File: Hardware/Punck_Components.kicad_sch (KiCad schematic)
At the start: 115 parts, among them J1 Conn_01x12_Female, J2 Conn_01x12_Female, J3 Conn_01x12_Female, J4 Conn_01x12_Female, J6 SWD_Header, J7 Eurorack_10_pin_power, Q1 MMBT3904, Q2 MMBT3904, Q3 MMBT3904, Q4 MMBT3904, Q5 MMBT3904, Q6 MMBT3904, Q7 MMBT3904, U1 TL074, U2 STM32H743ZITx, U3 W25Q128JVS, U4 PCM5100APW, U5 W25Q128JVS, U6 TPS561201, U7 LD1117-3.3-4Tab, Y1 8MHz 20pF

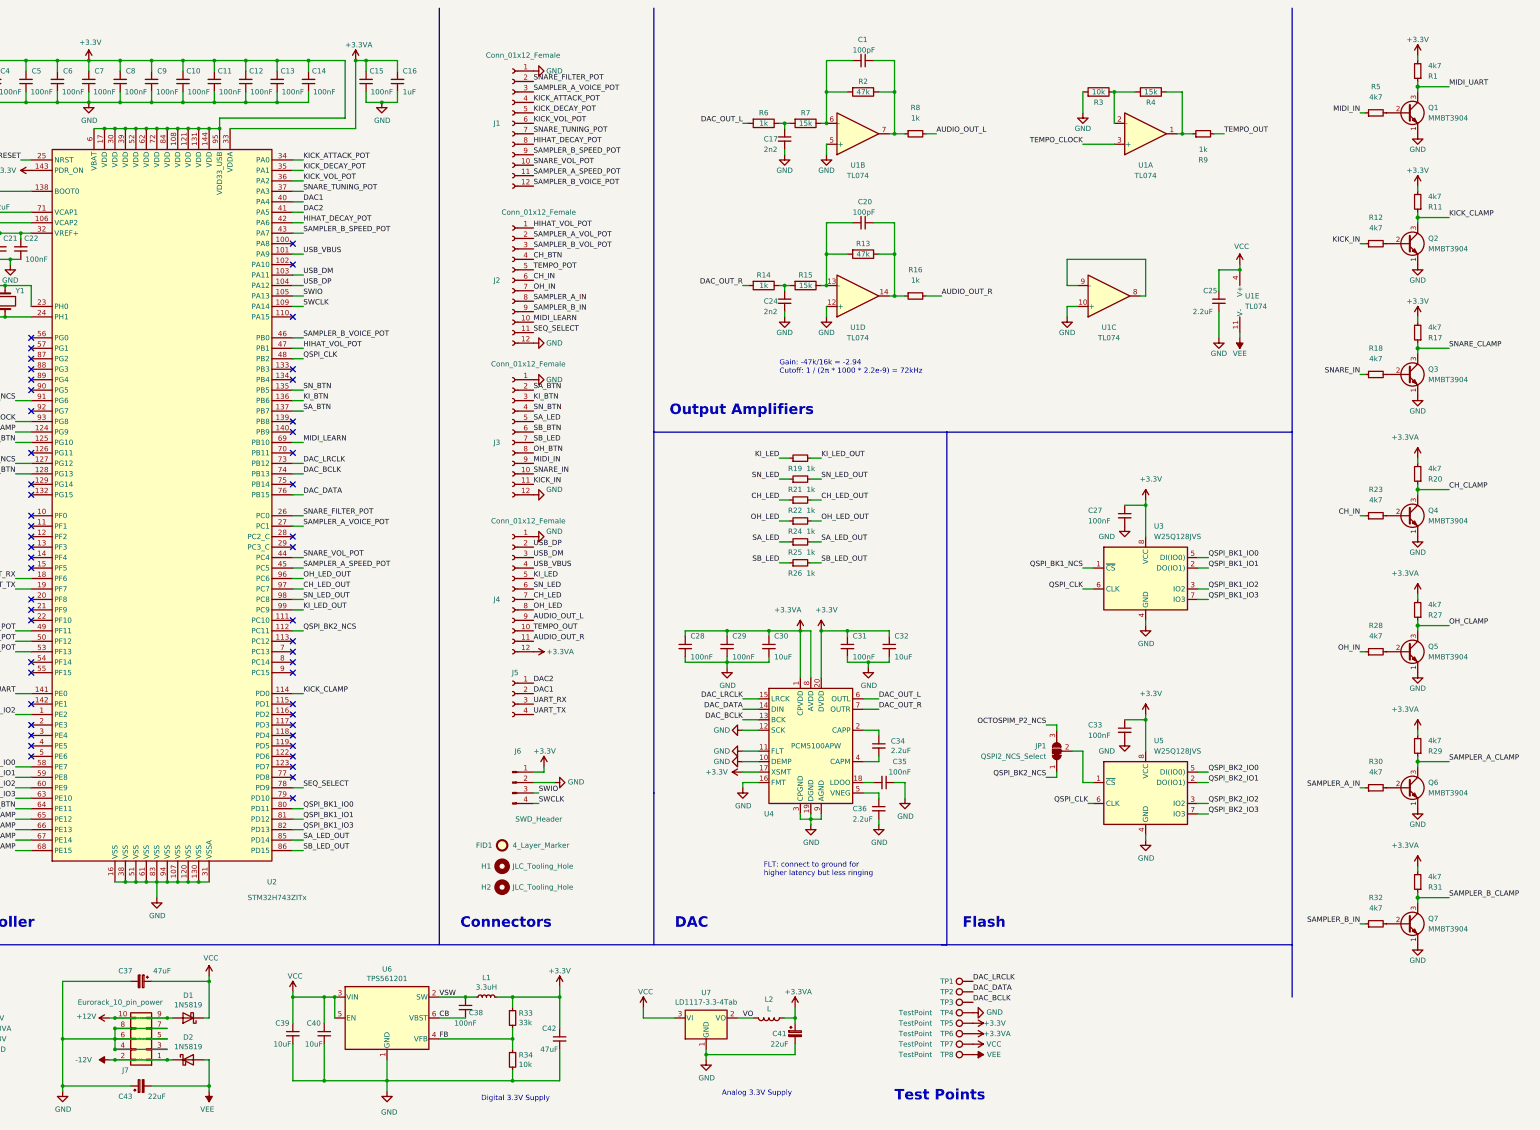
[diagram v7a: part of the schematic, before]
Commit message: Updated components on panel board
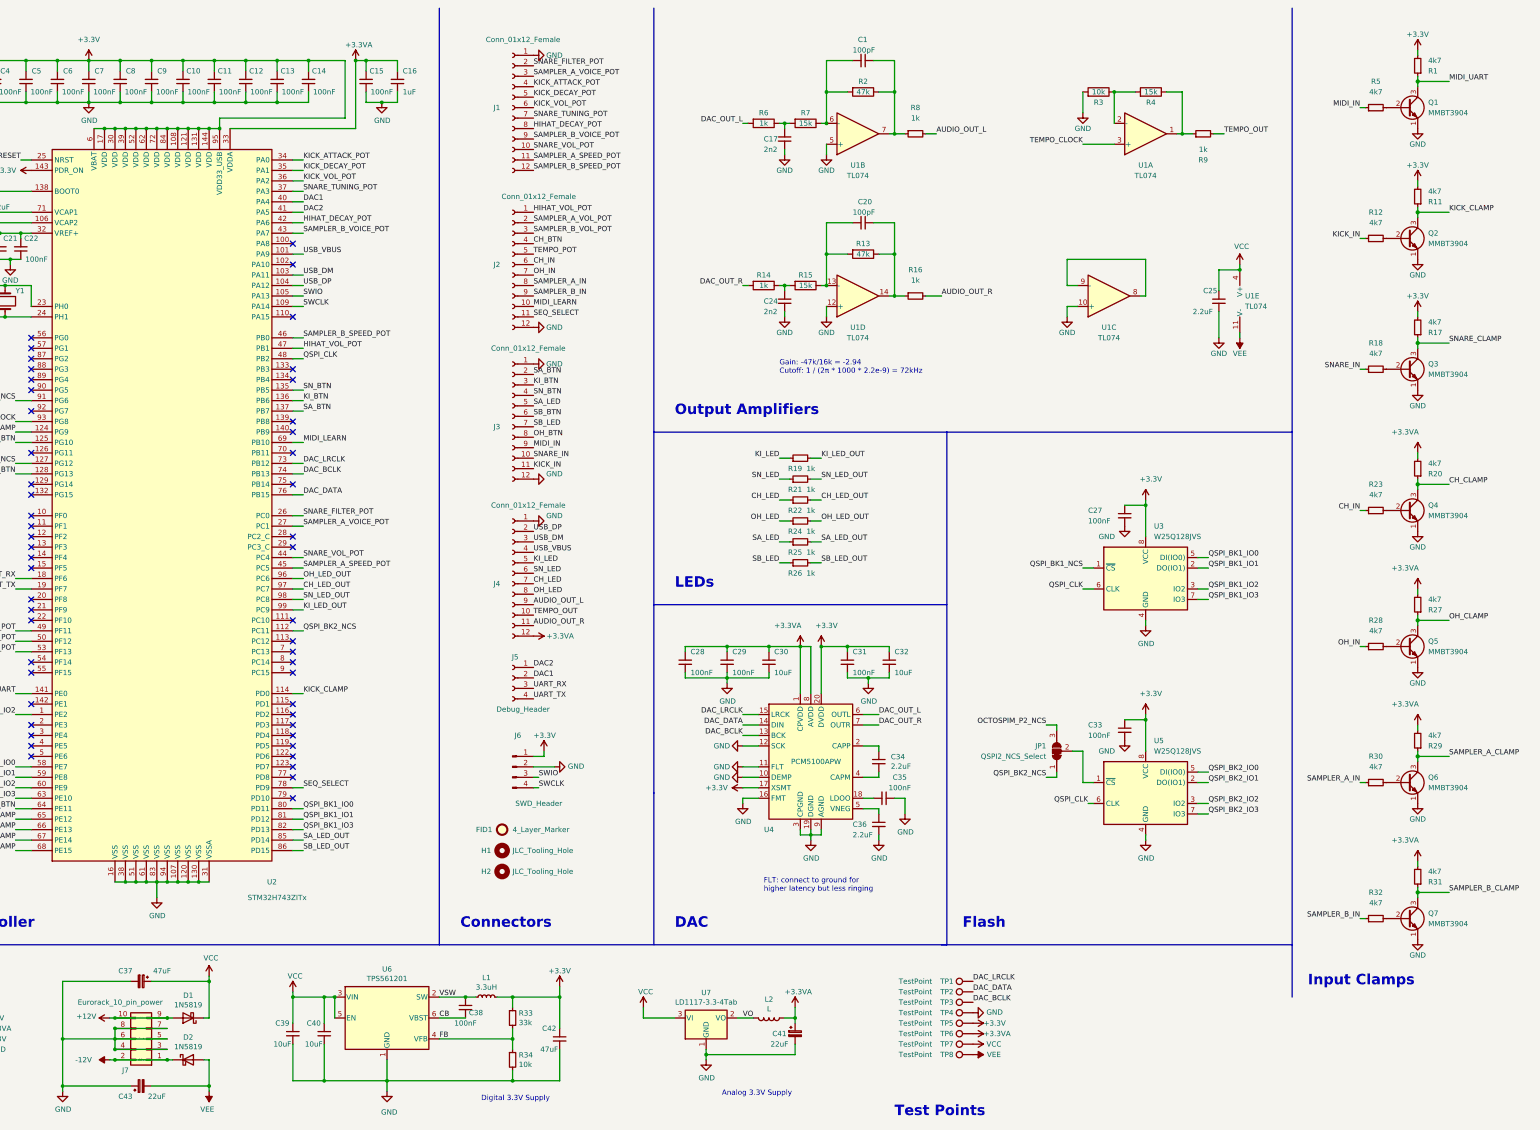
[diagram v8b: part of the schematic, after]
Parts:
- J5: value (none) -> Debug_Header
- TP1, TP2, TP3: value (none) -> TestPoint; footprint (none) -> Custom_Footprints:1.3mm_Test_Point
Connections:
- net +3V3: no longer C10.2, C11.2, C12.2, C13.2, C14.2, C2.2, C3.2, C31.1, C32.1, C4.2, C5.2, C6.2, C7.2, C8.2, C9.2, U2.108 (VDD), U2.121 (VDD), U2.131 (VDD), U2.144 (VDD), U2.17 (VDD), U2.30 (VDD), U2.39 (VDD), U2.52 (VDD), U2.6 (VBAT), U2.62 (VDD), U2.72 (VDD), U2.84 (VDD), U2.95 (VDD33_USB), U4.20 (DVDD)
- net SAMPLER_B_SPEED_POT: now also J1.12 (Pin_12), U2.46 (PB0); no longer J1.9 (Pin_9), U2.43 (PA7)
- net SAMPLER_B_VOICE_POT: now also J1.9 (Pin_9), U2.43 (PA7); no longer J1.12 (Pin_12), U2.46 (PB0)
- new net +3.3V: C10.2, C11.2, C12.2, C13.2, C14.2, C2.2, C3.2, C31.1, C32.1, C4.2, C5.2, C6.2, C7.2, C8.2, C9.2, U2.108 (VDD), U2.121 (VDD), U2.131 (VDD), U2.144 (VDD), U2.17 (VDD), U2.30 (VDD), U2.39 (VDD), U2.52 (VDD), U2.6 (VBAT), U2.62 (VDD), U2.72 (VDD), U2.84 (VDD), U2.95 (VDD33_USB), U4.20 (DVDD)
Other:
- note added: "Input Clamps"
- note added: "LEDs"
- title: Retrospector v3 -> Punck v1
- moved on the sheet: C28, C29, C30, C31, C32, C34, C35, C36, FID1, H1, H2, J1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
